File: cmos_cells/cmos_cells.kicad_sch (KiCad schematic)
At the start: 347 parts

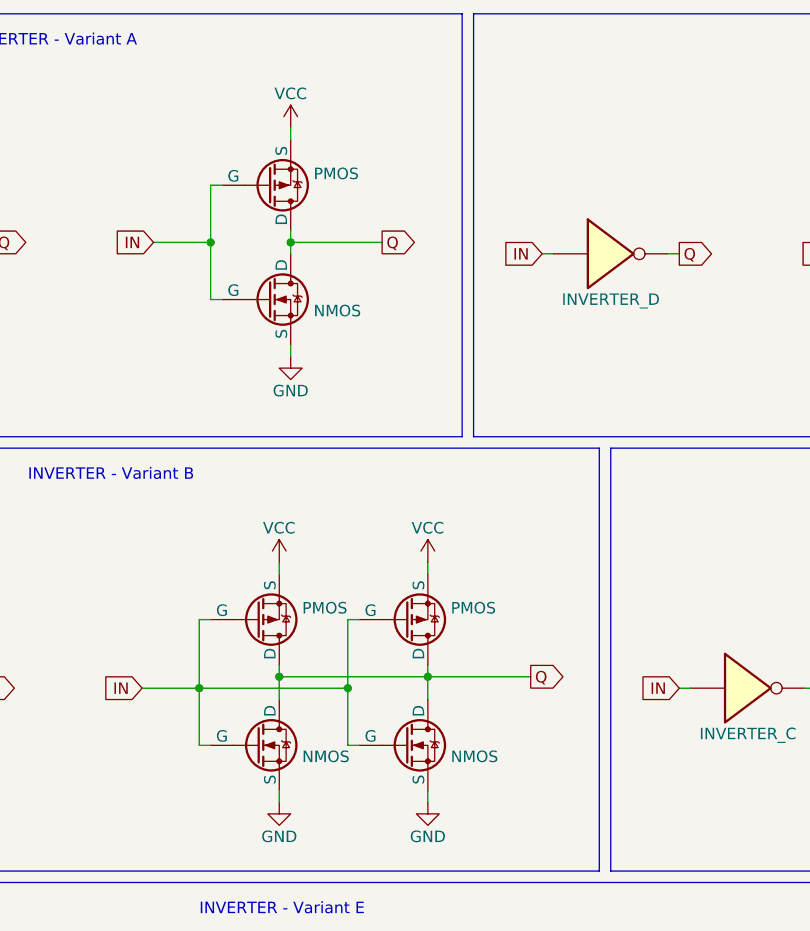
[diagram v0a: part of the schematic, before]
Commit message: Add cell layout for inverter variants A & B
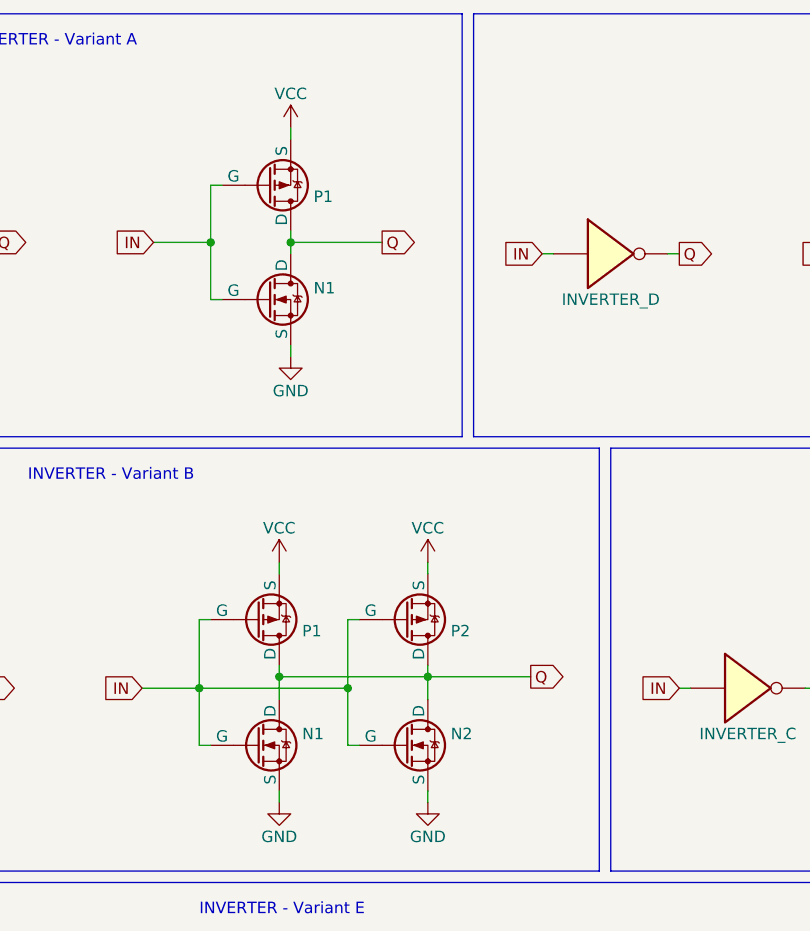
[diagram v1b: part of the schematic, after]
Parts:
- gave numbers to parts that had none: 4
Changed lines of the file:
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@@
   (symbol (lib_id "Device:Q_PMOS_DGS") (at 67.31 31.75 0) (mirror x) (unit 1)
     (in_bom yes) (on_board yes)
-    (property "Reference" "Q?" (id 0) (at 72.39 33.02 0)
-      (effects (font (size 1.27 1.27)) (justify left) hide)
+    (property "Reference" "P1" (id 0) (at 72.39 33.02 0)
+      (effects (font (size 1.27 1.27)) (justify left))
     )
     (property "Value" "PMOS" (id 1) (at 72.39 30.48 0)
-      (effects (font (size 1.27 1.27)) (justify left))
+      (effects (font (size 1.27 1.27)) (justify left) hide)
     )
     (property "Footprint" "" (id 2) (at 72.39 34.29 0)
@@
   (symbol (lib_name "Q_PMOS_DGS_2") (lib_id "Device:Q_PMOS_DGS") (at 82.55 80.01 0) (mirror x) (unit 1)
     (in_bom yes) (on_board yes)
-    (property "Reference" "Q?" (id 0) (at 87.63 81.28 0)
-      (effects (font (size 1.27 1.27)) (justify left) hide)
+    (property "Reference" "P2" (id 0) (at 87.63 81.28 0)
+      (effects (font (size 1.27 1.27)) (justify left))
     )
     (property "Value" "PMOS" (id 1) (at 87.63 78.74 0)
-      (effects (font (size 1.27 1.27)) (justify left))
+      (effects (font (size 1.27 1.27)) (justify left) hide)
     )
     (property "Footprint" "" (id 2) (at 87.63 82.55 0)
@@
   (symbol (lib_name "Q_NMOS_DGS_1") (lib_id "Device:Q_NMOS_DGS") (at 66.04 93.98 0) (unit 1)
     (in_bom yes) (on_board yes)
-    (property "Reference" "Q?" (id 0) (at 71.12 92.71 0)
-      (effects (font (size 1.27 1.27)) (justify left) hide)
+    (property "Reference" "N1" (id 0) (at 71.12 92.71 0)
+      (effects (font (size 1.27 1.27)) (justify left))
     )
     (property "Value" "NMOS" (id 1) (at 71.12 95.25 0)
-      (effects (font (size 1.27 1.27)) (justify left))
+      (effects (font (size 1.27 1.27)) (justify left) hide)
     )
     (property "Footprint" "" (id 2) (at 71.12 91.44 0)
@@
   (symbol (lib_name "Q_PMOS_DGS_1") (lib_id "Device:Q_PMOS_DGS") (at 66.04 80.01 0) (mirror x) (unit 1)
     (in_bom yes) (on_board yes)
-    (property "Reference" "Q?" (id 0) (at 71.12 81.28 0)
-      (effects (font (size 1.27 1.27)) (justify left) hide)
+    (property "Reference" "P1" (id 0) (at 71.12 81.28 0)
+      (effects (font (size 1.27 1.27)) (justify left))
     )
     (property "Value" "PMOS" (id 1) (at 71.12 78.74 0)
-      (effects (font (size 1.27 1.27)) (justify left))
+      (effects (font (size 1.27 1.27)) (justify left) hide)
     )
     (property "Footprint" "" (id 2) (at 71.12 82.55 0)
@@
   (symbol (lib_name "Q_NMOS_DGS_2") (lib_id "Device:Q_NMOS_DGS") (at 82.55 93.98 0) (unit 1)
     (in_bom yes) (on_board yes)
-    (property "Reference" "Q?" (id 0) (at 87.63 92.71 0)
-      (effects (font (size 1.27 1.27)) (justify left) hide)
+    (property "Reference" "N2" (id 0) (at 87.63 92.71 0)
+      (effects (font (size 1.27 1.27)) (justify left))
     )
     (property "Value" "NMOS" (id 1) (at 87.63 95.25 0)
-      (effects (font (size 1.27 1.27)) (justify left))
+      (effects (font (size 1.27 1.27)) (justify left) hide)
     )
     (property "Footprint" "" (id 2) (at 87.63 91.44 0)
@@
   (symbol (lib_id "Device:Q_NMOS_DGS") (at 67.31 44.45 0) (unit 1)
     (in_bom yes) (on_board yes)
-    (property "Reference" "Q?" (id 0) (at 72.39 43.18 0)
-      (effects (font (size 1.27 1.27)) (justify left) hide)
+    (property "Reference" "N1" (id 0) (at 72.39 43.18 0)
+      (effects (font (size 1.27 1.27)) (justify left))
     )
     (property "Value" "NMOS" (id 1) (at 72.39 45.72 0)
-      (effects (font (size 1.27 1.27)) (justify left))
+      (effects (font (size 1.27 1.27)) (justify left) hide)
     )
     (property "Footprint" "" (id 2) (at 72.39 41.91 0)
@@
       (reference "#PWR?") (unit 1) (value "GND") (footprint "")
     )
+    (path "/82c46efe-78c6-48ac-9f5c-8a3f5b74aada"
+      (reference "N1") (unit 1) (value "NMOS") (footprint "")
+    )
+    (path "/f9b1563b-384a-447c-9f47-736504e995c8"
+      (reference "N1") (unit 1) (value "NMOS") (footprint "")
+    )
+    (path "/f68d1688-39d3-4df3-a31f-66904ee7037e"
+      (reference "N2") (unit 1) (value "NMOS") (footprint "")
+    )
+    (path "/11b49d13-b047-4242-be65-9a9b1c80ec58"
+      (reference "P1") (unit 1) (value "PMOS") (footprint "")
+    )
+    (path "/ebd59515-0d58-4106-b813-48004cd7f826"
+      (reference "P1") (unit 1) (value "PMOS") (footprint "")
+    )
+    (path "/40823c7b-b947-4667-bacb-0fc1466caf82"
+      (reference "P2") (unit 1) (value "PMOS") (footprint "")
+    )
     (path "/009e67fa-12a5-4a8e-bac0-ef0aa380ed1d"
       (reference "Q?") (unit 1) (value "NMOS") (footprint "")
@@
       (reference "Q?") (unit 1) (value "NMOS") (footprint "")
     )
-    (path "/11b49d13-b047-4242-be65-9a9b1c80ec58"
-      (reference "Q?") (unit 1) (value "PMOS") (footprint "")
-    )
     (path "/11e06bd4-c7aa-45b3-82d9-3d09d670224d"
       (reference "Q?") (unit 1) (value "NMOS") (footprint "")
@@
       (reference "Q?") (unit 1) (value "PMOS") (footprint "")
     )
-    (path "/40823c7b-b947-4667-bacb-0fc1466caf82"
-      (reference "Q?") (unit 1) (value "PMOS") (footprint "")
-    )
     (path "/40b89b20-8178-4f03-b54d-fa5c749b0f82"
       (reference "Q?") (unit 1) (value "PMOS") (footprint "")
@@
       (reference "Q?") (unit 1) (value "PMOS") (footprint "")
     )
-    (path "/82c46efe-78c6-48ac-9f5c-8a3f5b74aada"
-      (reference "Q?") (unit 1) (value "NMOS") (footprint "")
-    )
     (path "/8366180c-5d62-4b29-adb9-b95f614edd1c"
       (reference "Q?") (unit 1) (value "PMOS") (footprint "")
@@
       (reference "Q?") (unit 1) (value "PMOS") (footprint "")
     )
-    (path "/ebd59515-0d58-4106-b813-48004cd7f826"
-      (reference "Q?") (unit 1) (value "PMOS") (footprint "")
-    )
     (path "/edb23856-43eb-4464-9642-c7eab84342cc"
       (reference "Q?") (unit 1) (value "PMOS") (footprint "")
@@
       (reference "Q?") (unit 1) (value "PMOS") (footprint "")
     )
-    (path "/f68d1688-39d3-4df3-a31f-66904ee7037e"
-      (reference "Q?") (unit 1) (value "NMOS") (footprint "")
-    )
     (path "/f8903ec5-9e0e-4aa1-89e2-17a60a4e010d"
       (reference "Q?") (unit 1) (value "PMOS") (footprint "")
     )
-    (path "/f9b1563b-384a-447c-9f47-736504e995c8"
-      (reference "Q?") (unit 1) (value "NMOS") (footprint "")
-    )
     (path "/f9cea6b9-a1ba-4ad2-ab19-3a49fae48142"

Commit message: Use new MOSFET symbols
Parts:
- removed N1 (x2), N2, Q? (x154): NMOS, symbol Device:Q_NMOS_DGS
- removed P1 (x2), P2, Q? (x154): PMOS, symbol Device:Q_PMOS_DGS
- removed U?: AOI, symbol DMG_CPU_Cells:AOI
- added N1 (x33), N10, N11, N12, N13, N2 (x32), N3 (x29), N4 (x23), N5 (x16), N6 (x9), N7 (x6), N8 (x4), N9 (x2): NMOS, symbol DMG_CPU_Cells:NMOS
- added P1 (x33), P10, P11, P12, P13, P2 (x32), P3 (x29), P4 (x23), P5 (x16), P6 (x9), P7 (x6), P8 (x4), P9 (x2): PMOS, symbol DMG_CPU_Cells:PMOS
- added U?: OAI, symbol DMG_CPU_Cells:OAI
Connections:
- net A: now also N2.2 (G), N4.2 (G), N8.2 (G), P3.2 (G), P5.2 (G), P8.2 (G)
- net B: now also N3.2 (G), N5.2 (G), N7.2 (G), P2.2 (G), P4.2 (G), P7.2 (G)
- net COUT: now also N1.1 (D), P1.1 (D)
- net GND: now also N1.3 (S), N1.3 (S), N1.3 (S), N1.3 (S), N1.3 (S), N1.3 (S), N1.3 (S), N1.3 (S), N1.3 (S), N1.3 (S), N1.3 (S), N1.3 (S), N1.3 (S), N1.3 (S), N1.3 (S), N1.3 (S), N1.3 (S), N1.3 (S), N1.3 (S), N1.3 (S), N1.3 (S), N1.3 (S), N1.3 (S), N1.3 (S), N1.3 (S), N1.3 (S), N1.3 (S), N1.3 (S), N1.3 (S), N1.3 (S), N1.3 (S), N11.3 (S), N13.3 (S), N2.3 (S), N2.3 (S), N2.3 (S), N2.3 (S), N2.3 (S), N2.3 (S), N2.3 (S), N2.3 (S), N2.3 (S), N2.3 (S), N2.3 (S), N2.3 (S), N2.3 (S), N2.3 (S), N2.3 (S), N2.3 (S), N2.3 (S), N3.3 (S), N3.3 (S), N3.3 (S), N3.3 (S), N3.3 (S), N3.3 (S), N3.3 (S), N3.3 (S), N3.3 (S), N3.3 (S), N3.3 (S), N3.3 (S), N3.3 (S), N3.3 (S), N3.3 (S), N3.3 (S), N3.3 (S), N3.3 (S), N3.3 (S), N3.3 (S), N4.3 (S), N4.3 (S), N4.3 (S), N4.3 (S), N4.3 (S), N4.3 (S), N4.3 (S), N4.3 (S), N4.3 (S), N4.3 (S), N4.3 (S), N4.3 (S), N5.3 (S), N5.3 (S), N5.3 (S), N5.3 (S), N5.3 (S), N5.3 (S), N5.3 (S), N5.3 (S), N5.3 (S), N5.3 (S), N5.3 (S), N5.3 (S), N5.3 (S), N6.3 (S), N6.3 (S), N6.3 (S), N6.3 (S), N7.3 (S), N7.3 (S), N7.3 (S), N7.3 (S), N7.3 (S), N8.3 (S), N8.3 (S), N9.3 (S), N9.3 (S)
- net IN: now also N1.2 (G), N1.2 (G), N1.2 (G), N1.2 (G), N1.2 (G), N2.2 (G), N2.2 (G), N2.2 (G), N2.2 (G), N3.2 (G), N3.2 (G), N3.2 (G), N4.2 (G), N4.2 (G), N5.2 (G), N6.2 (G), P1.2 (G), P1.2 (G), P1.2 (G), P1.2 (G), P1.2 (G), P2.2 (G), P2.2 (G), P2.2 (G), P2.2 (G), P3.2 (G), P3.2 (G), P3.2 (G), P4.2 (G), P4.2 (G), P5.2 (G), P6.2 (G)
- net IN1: now also N1.2 (G), N1.2 (G), N1.2 (G), N1.2 (G), N1.2 (G), N1.2 (G), N1.2 (G), N1.2 (G), N1.2 (G), N1.2 (G), N1.2 (G), N1.2 (G), N1.2 (G), N1.2 (G), N1.2 (G), N1.2 (G), N1.2 (G), N1.2 (G), N1.2 (G), N1.2 (G), N1.2 (G), N1.2 (G), N1.2 (G), N1.2 (G), N1.2 (G), N1.2 (G), N2.2 (G), N4.2 (G), N5.2 (G), P1.2 (G), P1.2 (G), P1.2 (G), P1.2 (G), P1.2 (G), P1.2 (G), P1.2 (G), P1.2 (G), P1.2 (G), P1.2 (G), P1.2 (G), P1.2 (G), P1.2 (G), P1.2 (G), P1.2 (G), P1.2 (G), P2.2 (G), P2.2 (G), P2.2 (G), P2.2 (G), P3.2 (G), P3.2 (G), P4.2 (G), P4.2 (G), P5.2 (G), P5.2 (G), P5.2 (G), P6.2 (G), P7.2 (G), U?.1
- net IN10: now also N10.2 (G), P11.2 (G)
- net IN11: now also N11.2 (G), P6.2 (G)
- net IN12: now also N12.2 (G), P12.2 (G)
- net IN2: now also N2.2 (G), N2.2 (G), N2.2 (G), N2.2 (G), N2.2 (G), N2.2 (G), N2.2 (G), N2.2 (G), N2.2 (G), N2.2 (G), N2.2 (G), N2.2 (G), N2.2 (G), N2.2 (G), N2.2 (G), N2.2 (G), N2.2 (G), N2.2 (G), N2.2 (G), N2.2 (G), N2.2 (G), N2.2 (G), N2.2 (G), N2.2 (G), N2.2 (G), N2.2 (G), N3.2 (G), N4.2 (G), N5.2 (G), P1.2 (G), P1.2 (G), P1.2 (G), P2.2 (G), P2.2 (G), P2.2 (G), P2.2 (G), P2.2 (G), P2.2 (G), P2.2 (G), P2.2 (G), P2.2 (G), P2.2 (G), P2.2 (G), P2.2 (G), P2.2 (G), P2.2 (G), P3.2 (G), P3.2 (G), P3.2 (G), P3.2 (G), P4.2 (G), P4.2 (G), P4.2 (G), P4.2 (G), P5.2 (G), P5.2 (G), P6.2 (G), P7.2 (G), U?.2
- net IN3: now also N3.2 (G), N3.2 (G), N3.2 (G), N3.2 (G), N3.2 (G), N3.2 (G), N3.2 (G), N3.2 (G), N3.2 (G), N3.2 (G), N3.2 (G), N3.2 (G), N3.2 (G), N3.2 (G), N3.2 (G), N3.2 (G), N3.2 (G), N3.2 (G), N3.2 (G), N3.2 (G), N3.2 (G), P1.2 (G), P1.2 (G), P2.2 (G), P2.2 (G), P2.2 (G), P2.2 (G), P2.2 (G), P2.2 (G), P3.2 (G), P3.2 (G), P3.2 (G), P3.2 (G), P3.2 (G), P3.2 (G), P3.2 (G), P3.2 (G), P3.2 (G), P3.2 (G), P3.2 (G), P4.2 (G), P5.2 (G), U?.3
- net IN4: now also N4.2 (G), N4.2 (G), N4.2 (G), N4.2 (G), N4.2 (G), N4.2 (G), N4.2 (G), N4.2 (G), N4.2 (G), N4.2 (G), N4.2 (G), N4.2 (G), N4.2 (G), N4.2 (G), P1.2 (G), P1.2 (G), P2.2 (G), P3.2 (G), P4.2 (G), P4.2 (G), P4.2 (G), P4.2 (G), P4.2 (G), P4.2 (G), P4.2 (G), P5.2 (G), P6.2 (G), P8.2 (G)
- net IN5: now also N5.2 (G), N5.2 (G), N5.2 (G), N5.2 (G), N5.2 (G), N5.2 (G), N5.2 (G), N5.2 (G), N5.2 (G), P1.2 (G), P2.2 (G), P3.2 (G), P3.2 (G), P3.2 (G), P3.2 (G), P5.2 (G), P5.2 (G), P5.2 (G)
- net IN6: now also N6.2 (G), N6.2 (G), N6.2 (G), N6.2 (G), N6.2 (G), N6.2 (G), N6.2 (G), P1.2 (G), P2.2 (G), P6.2 (G), P6.2 (G), P6.2 (G), P7.2 (G), P9.2 (G)
- net IN7: now also N7.2 (G), N7.2 (G), N7.2 (G), N7.2 (G), P1.2 (G), P4.2 (G), P4.2 (G), P7.2 (G)
- net IN8: now also N8.2 (G), N8.2 (G), N8.2 (G), P10.2 (G), P8.2 (G), P8.2 (G)
- net IN9: now also N9.2 (G), P5.2 (G)
- net Q: now also N1.1 (D), N1.1 (D), N1.1 (D), N1.1 (D), N1.1 (D), N1.1 (D), N1.1 (D), N1.1 (D), N1.1 (D), N1.1 (D), N1.1 (D), N1.1 (D), N1.1 (D), N13.1 (D), N2.1 (D), N2.1 (D), N2.1 (D), N2.1 (D), N2.1 (D), N2.1 (D), N2.1 (D), N2.1 (D), N2.1 (D), N2.1 (D), N2.1 (D), N3.1 (D), N3.1 (D), N3.1 (D), N3.1 (D), N3.1 (D), N3.1 (D), N3.1 (D), N3.1 (D), N3.1 (D), N3.1 (D), N3.1 (D), N3.1 (D), N3.1 (D), N4.1 (D), N4.1 (D), N4.1 (D), N4.1 (D), N4.1 (D), N4.1 (D), N4.1 (D), N4.1 (D), N4.1 (D), N4.1 (D), N4.1 (D), N5.1 (D), N5.1 (D), N5.1 (D), N5.1 (D), N5.1 (D), N5.1 (D), N5.1 (D), N5.1 (D), N6.1 (D), N6.1 (D), N6.1 (D), N6.1 (D), N7.1 (D), N7.1 (D), N7.1 (D), N8.1 (D), N9.1 (D), P1.1 (D), P1.1 (D), P1.1 (D), P1.1 (D), P1.1 (D), P1.1 (D), P1.1 (D), P1.1 (D), P1.1 (D), P1.1 (D), P1.1 (D), P1.1 (D), P1.1 (D), P13.1 (D), P2.1 (D), P2.1 (D), P2.1 (D), P2.1 (D), P2.1 (D), P2.1 (D), P2.1 (D), P2.1 (D), P2.1 (D), P2.1 (D), P2.1 (D), P2.1 (D), P2.1 (D), P2.1 (D), P3.1 (D), P3.1 (D), P3.1 (D), P3.1 (D), P3.1 (D), P3.1 (D), P3.1 (D), P3.1 (D), P3.1 (D), P3.1 (D), P3.1 (D), P3.1 (D), P4.1 (D), P4.1 (D), P4.1 (D), P4.1 (D), P4.1 (D), P4.1 (D), P4.1 (D), P4.1 (D), P4.1 (D), P4.1 (D), P4.1 (D), P5.1 (D), P5.1 (D), P5.1 (D), P5.1 (D), P5.1 (D), P5.1 (D), P5.1 (D), P5.1 (D), P6.1 (D), P6.1 (D), P6.1 (D), P6.1 (D), P7.1 (D), P7.1 (D), P8.1 (D), P9.1 (D), U?.4
- net SUM: now also N4.1 (D), N6.1 (D), P4.1 (D), P5.1 (D)
- net VCC: now also P1.3 (S), P1.3 (S), P1.3 (S), P1.3 (S), P1.3 (S), P1.3 (S), P1.3 (S), P1.3 (S), P1.3 (S), P1.3 (S), P1.3 (S), P1.3 (S), P1.3 (S), P1.3 (S), P1.3 (S), P1.3 (S), P1.3 (S), P1.3 (S), P1.3 (S), P1.3 (S), P1.3 (S), P1.3 (S), P1.3 (S), P1.3 (S), P1.3 (S), P1.3 (S), P1.3 (S), P1.3 (S), P1.3 (S), P1.3 (S), P1.3 (S), P1.3 (S), P13.3 (S), P2.3 (S), P2.3 (S), P2.3 (S), P2.3 (S), P2.3 (S), P2.3 (S), P2.3 (S), P2.3 (S), P2.3 (S), P2.3 (S), P2.3 (S), P2.3 (S), P2.3 (S), P2.3 (S), P2.3 (S), P3.3 (S), P3.3 (S), P3.3 (S), P3.3 (S), P3.3 (S), P3.3 (S), P3.3 (S), P3.3 (S), P3.3 (S), P3.3 (S), P3.3 (S), P3.3 (S), P3.3 (S), P3.3 (S), P3.3 (S), P3.3 (S), P3.3 (S), P3.3 (S), P4.3 (S), P4.3 (S), P4.3 (S), P4.3 (S), P4.3 (S), P4.3 (S), P4.3 (S), P4.3 (S), P4.3 (S), P4.3 (S), P4.3 (S), P4.3 (S), P4.3 (S), P5.3 (S), P5.3 (S), P5.3 (S), P5.3 (S), P5.3 (S), P5.3 (S), P5.3 (S), P5.3 (S), P5.3 (S), P5.3 (S), P6.3 (S), P6.3 (S), P6.3 (S), P6.3 (S), P7.3 (S), P7.3 (S), P7.3 (S), P8.3 (S), P9.3 (S)
- new net: P2.3 (S), P3.1 (D)
- new net: N1.2 (G), N2.1 (D), P1.2 (G), P2.1 (D), P3.1 (D)
- new net: P11.1 (D), P12.3 (S), P5.1 (D), P6.3 (S)
- new net: P10.1 (D), P11.3 (S), P4.1 (D), P5.3 (S)
- new net: N10.1 (D), N12.1 (D), N13.2 (G), N2.1 (D), N4.1 (D), N6.1 (D), N8.1 (D), P12.1 (D), P13.2 (G), P6.1 (D)
- new net: N5.1 (D), N6.3 (S) (x5)
- new net: N2.1 (D), N3.3 (S) (x7)
- new net: N1.1 (D), N2.3 (S) (x14)
- new net: P2.1 (D), P3.3 (S) (x7)
- new net: P1.1 (D), P2.3 (S) (x11)
- new net: N2.1 (D), N4.1 (D), N6.1 (D), N8.1 (D), N9.2 (G), P4.1 (D), P8.1 (D), P9.2 (G)
- new net: N7.1 (D), N8.3 (S) (x2)
- new net: P7.3 (S), P8.1 (D)
- new net: N1.1 (D), N2.1 (D), N3.3 (S) (x2)
- new net: N1.1 (D), N2.1 (D), N3.1 (D), N4.1 (D), N5.2 (G), P4.1 (D), P5.2 (G)
- new net: N3.2 (G), N4.1 (D), N5.1 (D), P3.2 (G), P4.1 (D)
- new net: N4.3 (S), N5.1 (D) (x2)
- new net: N3.1 (D), N4.2 (G), P1.1 (D), P2.1 (D), P3.1 (D), P4.2 (G)
- new net: N2.1 (D), N4.1 (D), N6.1 (D), N7.2 (G), P3.1 (D), P6.1 (D), P7.2 (G)
- new net: N1.2 (G), N4.1 (D), P1.2 (G), P4.1 (D), P5.1 (D)
- new net: P2.1 (D), P3.3 (S), P5.1 (D), P6.3 (S)
- new net: N3.1 (D), N4.3 (S) (x9)
- new net: N6.1 (D), N7.3 (S)
- new net: N1.1 (D), N2.1 (D), N3.1 (D), N4.2 (G), P3.1 (D), P4.2 (G)
- new net: N4.1 (D), N5.2 (G), P1.1 (D), P2.1 (D), P3.1 (D), P4.1 (D), P5.2 (G)
- new net: P2.1 (D), P3.3 (S), P8.1 (D), P9.3 (S)
- new net: P1.1 (D), P2.3 (S), P7.1 (D), P8.3 (S)
- new net: P1.1 (D), P2.3 (S), P3.1 (D), P4.3 (S)
- new net: N10.3 (S), N9.1 (D)
- new net: P4.1 (D), P5.3 (S) (x3)
- new net: P3.1 (D), P4.3 (S) (x5)
- new net: P1.1 (D), P2.3 (S), P4.1 (D), P5.3 (S)
- new net: N2.1 (D), N3.2 (G), P1.1 (D), P2.1 (D), P3.2 (G)
- new net: N4.1 (D), N5.3 (S) (x3)
- new net: N1.1 (D), N2.1 (D), N3.2 (G), P2.1 (D), P3.2 (G)
- new net: N2.1 (D), N3.1 (D), N4.2 (G), P3.1 (D), P4.2 (G)
- new net: P1.1 (D), P2.1 (D), P3.3 (S)
- new net: P10.3 (S), P3.1 (D), P4.3 (S), P9.1 (D)
- new net: P3.1 (D), P4.3 (S), P7.1 (D), P8.3 (S)
- new net: P2.1 (D), P3.3 (S), P6.1 (D), P7.3 (S)
- new net: P5.1 (D), P6.3 (S) (x2)
- new net: P1.1 (D), P2.3 (S), P5.1 (D), P6.3 (S)
- new net: N2.1 (D), N4.1 (D), N5.2 (G), P2.1 (D), P4.1 (D), P5.2 (G)
- new net: P4.3 (S), P5.3 (S), P6.1 (D)
- new net: N6.2 (G), N7.1 (D), N8.1 (D), P6.2 (G), P7.1 (D)
- new net: N3.1 (D), N4.2 (G), P2.1 (D), P3.1 (D), P4.2 (G)
- new net: P4.3 (S), P5.1 (D)
- new net: P6.1 (D), P7.3 (S)
- new net: N1.3 (S), N2.1 (D)
- new net: N2.3 (S), N3.1 (D)
- new net: N1.3 (S), N2.1 (D), N3.1 (D)
- new net: P1.3 (S), P2.3 (S), P3.1 (D)
- new net: P7.1 (D), P8.3 (S)
- new net: N11.1 (D), N12.3 (S)
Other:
- note added: "OAI"
- note removed: "AOI"

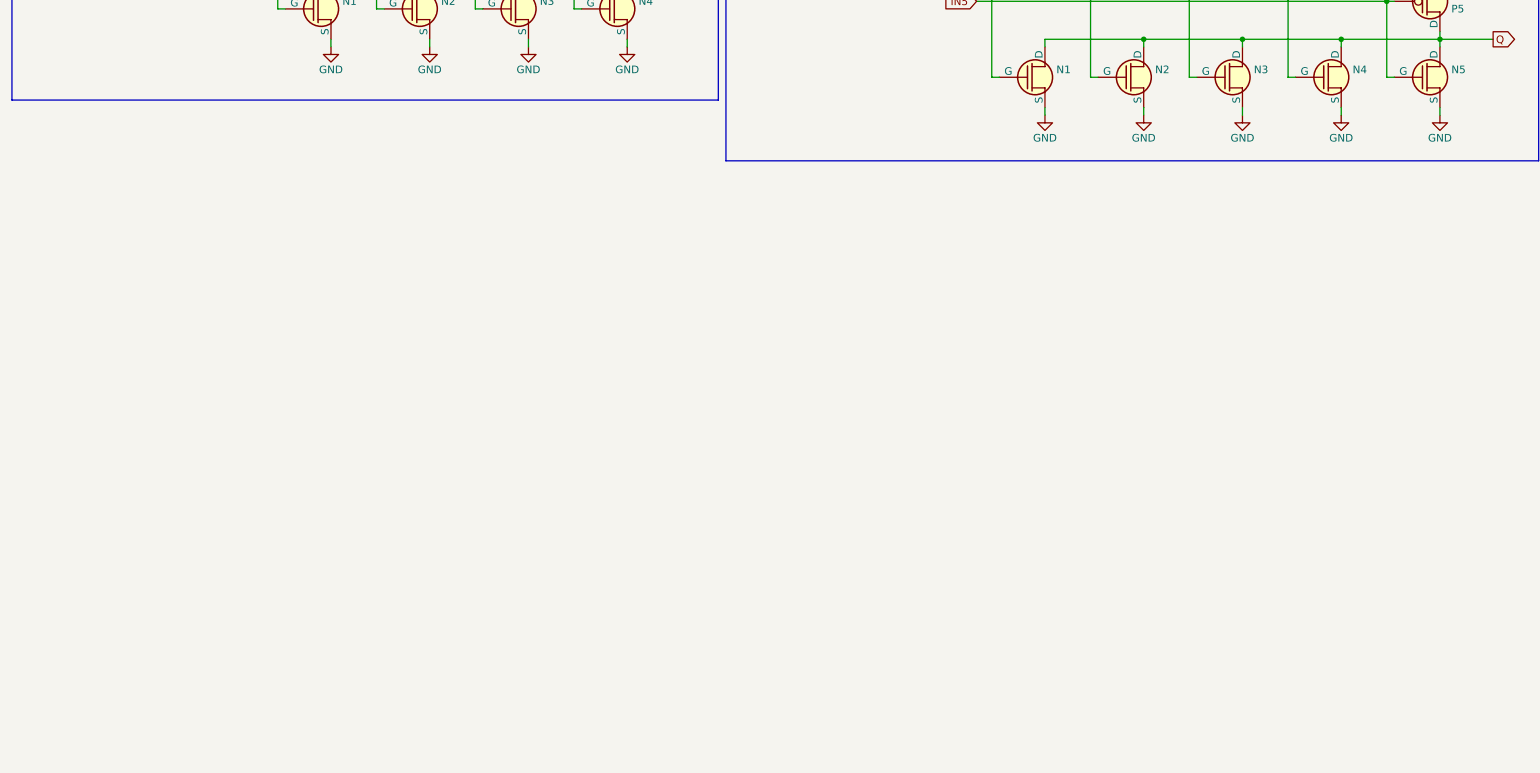
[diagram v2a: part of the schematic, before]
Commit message: Add schematic for MUX and MUXI cells
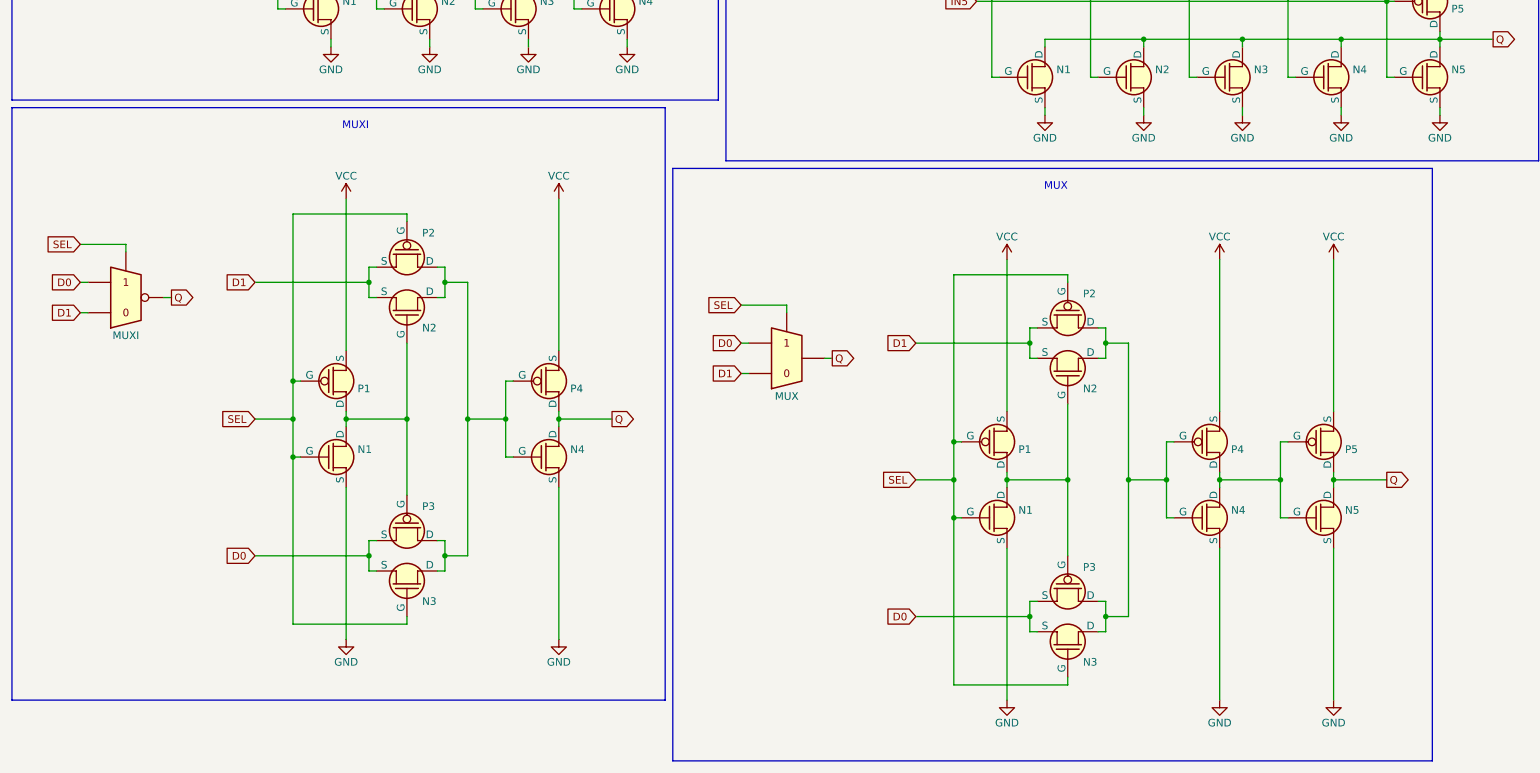
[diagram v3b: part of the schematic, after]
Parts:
- added N1 (x2), N2 (x2), N3 (x2), N4 (x2), N5: NMOS, symbol DMG_CPU_Cells:NMOS
- added P1 (x2), P2 (x2), P3 (x2), P4 (x2), P5: PMOS, symbol DMG_CPU_Cells:PMOS
- added U?: MUX, symbol DMG_CPU_Cells:MUX
- added U?: MUXI, symbol DMG_CPU_Cells:MUXI
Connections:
- net GND: now also N1.3 (S), N1.3 (S), N4.3 (S), N4.3 (S), N5.3 (S)
- net Q: now also N4.1 (D), N5.1 (D), P4.1 (D), P5.1 (D), U?.4, U?.4
- net VCC: now also P1.3 (S), P1.3 (S), P4.3 (S), P4.3 (S), P5.3 (S)
- new net: N4.1 (D), N5.2 (G), P4.1 (D), P5.2 (G)
- new net: N2.1 (D), N3.1 (D), N4.2 (G), P2.1 (D), P3.1 (D), P4.2 (G) (x2)
- new net: N1.1 (D), N2.2 (G), P1.1 (D), P3.2 (G) (x2)
- new net D0: N3.3 (S), N3.3 (S), P3.3 (S), P3.3 (S), U?.2, U?.2
- new net D1: N2.3 (S), N2.3 (S), P2.3 (S), P2.3 (S), U?.3, U?.3
- new net SEL: N1.2 (G), N1.2 (G), N3.2 (G), N3.2 (G), P1.2 (G), P1.2 (G), P2.2 (G), P2.2 (G), U?.1, U?.1
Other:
- note added: "MUX"
- note added: "MUXI"
